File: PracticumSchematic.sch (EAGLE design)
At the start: 9 parts, among them U1 328P, U2 MMA8452Q, U3 SN74HC595N, U4 SN74HC595N, U5 SN74HC595N, U6 SN74HC595N

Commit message: Add files via upload
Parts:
- removed U3, U4, U5, U6: SN74HC595N, SparkFun-IC-Logic:74HC595N
- added R1, R2, R3, R4, R5, R6, R7, R8: 200, SparkFun-Resistors:200OHM-0603-1/10W-1%
- added U$1: MAX7219DIP, SparkFun-Retired:MAX7219DIP
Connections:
- new net N$1: LED1.K1, U$1.SEGDP
- new net N$10: R2.1, U$1.DIG1
- new net N$11: R3.1, U$1.DIG2
- new net N$12: R4.1, U$1.DIG3
- new net N$13: R5.1, U$1.DIG4
- new net N$14: R6.1, U$1.DIG5
- new net N$15: R7.1, U$1.DIG6
- new net N$16: R8.1, U$1.DIG7
- new net N$17: U$1.DIN, U1.PC3(ADC3)
- new net N$18: U1.PC5(ADC5/SCL), U2.SCL
- new net N$19: U1.PC4(ADC4/SDA), U2.SDA
- new net N$2: LED1.K2, U$1.SEGA
- new net N$20: U$1.LOAD, U1.PB2(SS/OC1B)
- new net N$21: R1.1, U$1.DIG0
- new net N$22: LED1.A2, R2.2
- new net N$23: LED1.A3, R3.2
- new net N$24: LED1.A4, R4.2
- new net N$25: LED1.A5, R5.2
- new net N$26: LED1.A6, R6.2
- new net N$27: LED1.A7, R7.2
- new net N$28: LED1.A8, R8.2
- new net N$3: LED1.K3, U$1.SEGB
- new net N$4: LED1.K4, U$1.SEGC
- new net N$5: LED1.K5, U$1.SEGD
- new net N$6: LED1.K6, U$1.SEGE
- new net N$7: LED1.K7, U$1.SEGF
- new net N$8: LED1.K8, U$1.SEGG
- new net N$9: LED1.A1, R1.2
- net GND: now also U$1.GND, U$1.GND2, U2.GND@0, U2.GND@1, U2.GND@2
- net SCK: now also U$1.CLK
- net VCC: now also U$1.VCC, U2.VDD
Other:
- note added: "MAX7219 LED Driver"
- note removed: "Shift Register"
- moved on the sheet: LED1, U1, U2

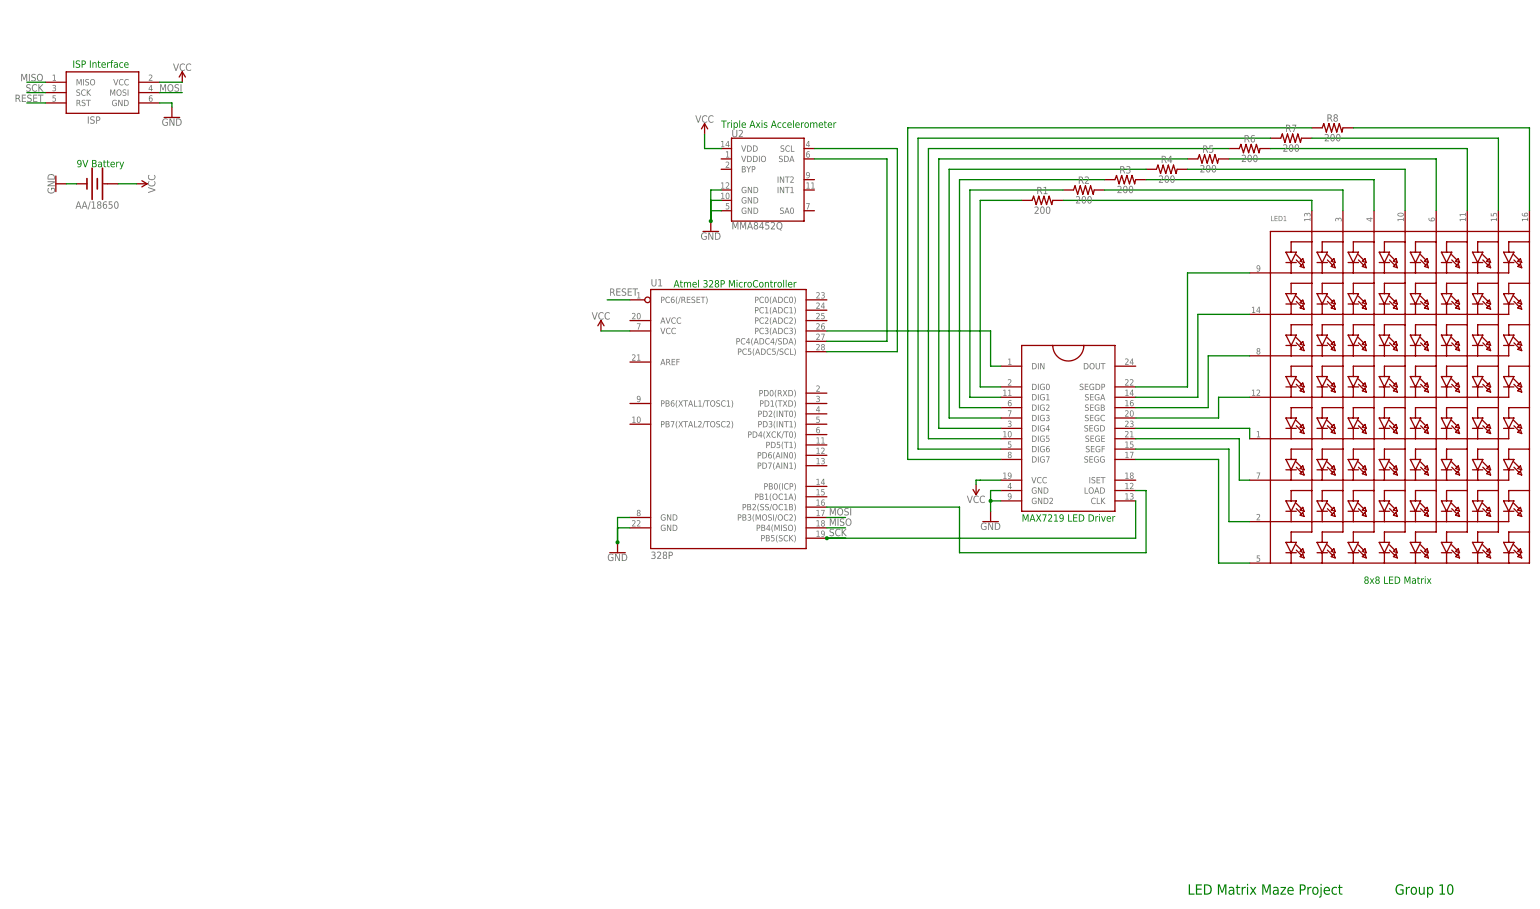
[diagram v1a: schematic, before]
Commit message: Update PracticumSchematic
Added pullup resistors to I2c. Added bypass capacitors to power supplies. Connected unused pins to Vcc. Connected SA0 pin on MMA8452 to ground. Added resistor to Vcc on Iset on MAX7219. Rotated battery.
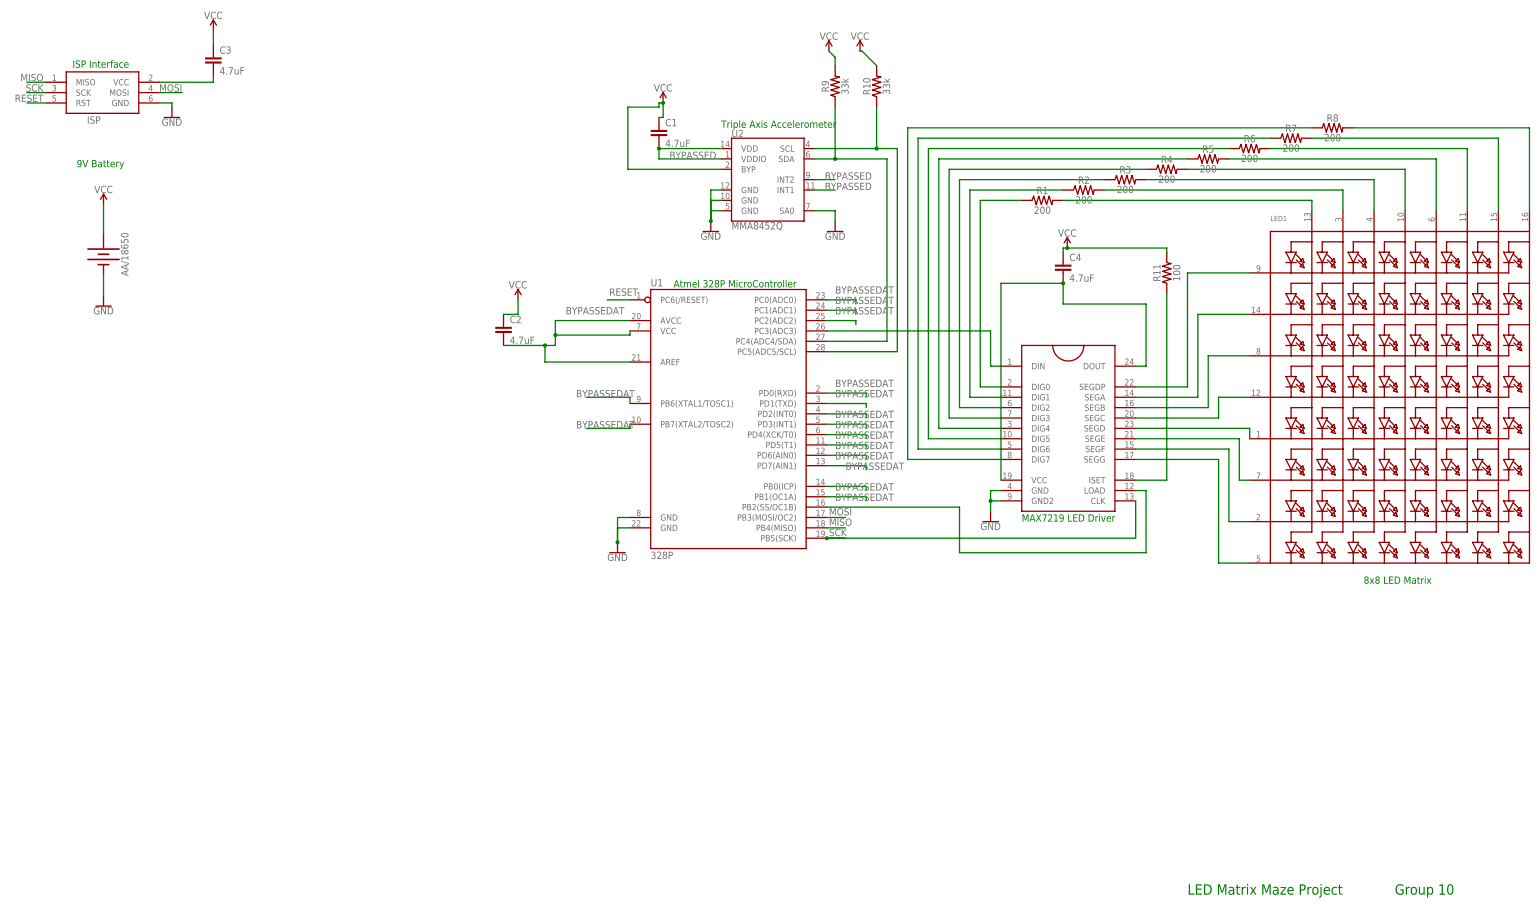
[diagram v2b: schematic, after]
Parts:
- added C1, C2, C3, C4: 4.7uF, SparkFun-Capacitors:4.7UF0603
- added R10, R9: 33k, SparkFun-Resistors:33KOHM-0603-1/10W-1%
- added R11: 100, SparkFun-Resistors:100OHM-0603-1/4W-5%
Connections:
- new net BYPASSED: C1.2, U2.INT1, U2.INT2, U2.VDD, U2.VDDIO
- new net BYPASSEDAT: C2.2, U1.AREF, U1.AVCC, U1.PB0(ICP), U1.PB1(OC1A), U1.PB6(XTAL1/TOSC1), U1.PB7(XTAL2/TOSC2), U1.PC0(ADC0), U1.PC1(ADC1), U1.PC2(ADC2), U1.PD0(RXD), U1.PD1(TXD), U1.PD2(INT0), U1.PD3(INT1), U1.PD4(XCK/T0), U1.PD5(T1), U1.PD6(AIN0), U1.PD7(AIN1), U1.VCC
- new net N$29: C3.2, ISP.VCC
- new net N$30: C4.2, U$1.DOUT, U$1.VCC
- new net N$32: R11.1, U$1.ISET
- net GND: now also U2.SA0
- net N$18: now also R10.1
- net N$19: now also R9.1
- net VCC: now also C1.1, C2.1, C3.1, C4.1, R10.2, R11.2, R9.2, U2.BYP; no longer ISP.VCC, U$1.VCC, U1.VCC, U2.VDD
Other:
- moved on the sheet: AA/18650
